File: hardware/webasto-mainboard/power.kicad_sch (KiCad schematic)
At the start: 14 parts, among them U5 BD9G341EFJ

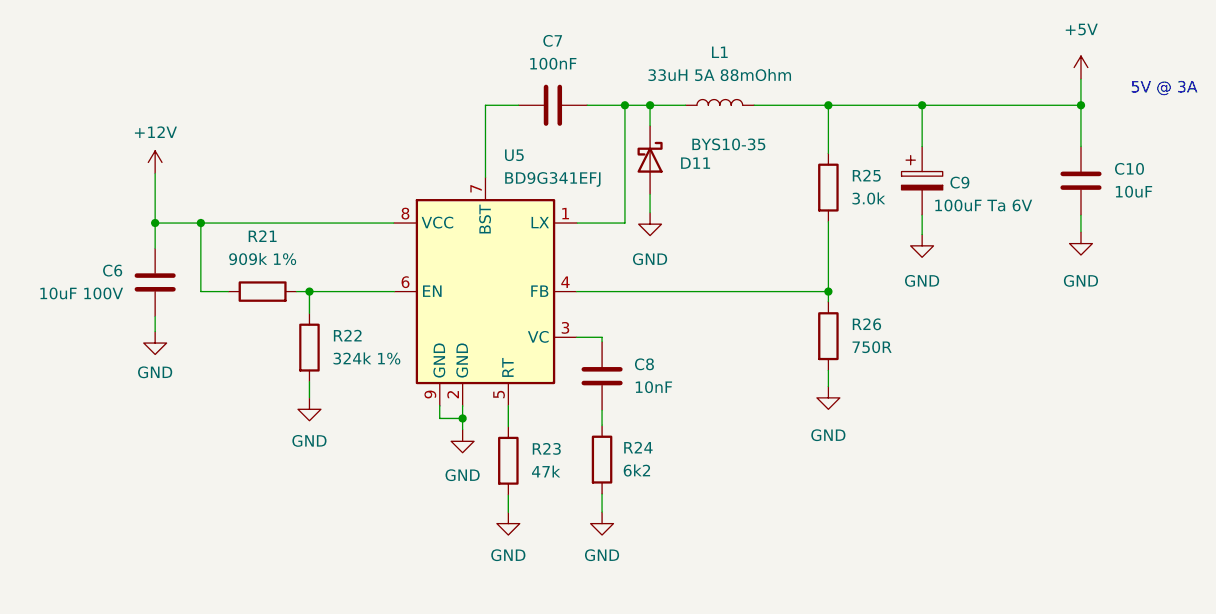
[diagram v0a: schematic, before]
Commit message: Move start/run to sensor board, add CANBUS
- WiFi is not being very helpful, and I'm concerned it won't work well once
  installed in the bus...  CANBus wiring is easy.
- Removed both Start/Run and the Vehicle Fan Relay from X1 to make space for
  canbus
- moved LEDs onto an I2C gpio extender.
- will need to still plumb in CAN_EN support
- will also need to yank out the WiFi stuff that won't stay stable anyways
  and reroute the CBOR out the CANBus instead of WiFi
- Vehicle Fan control will need to move to a LINBus fan controller board
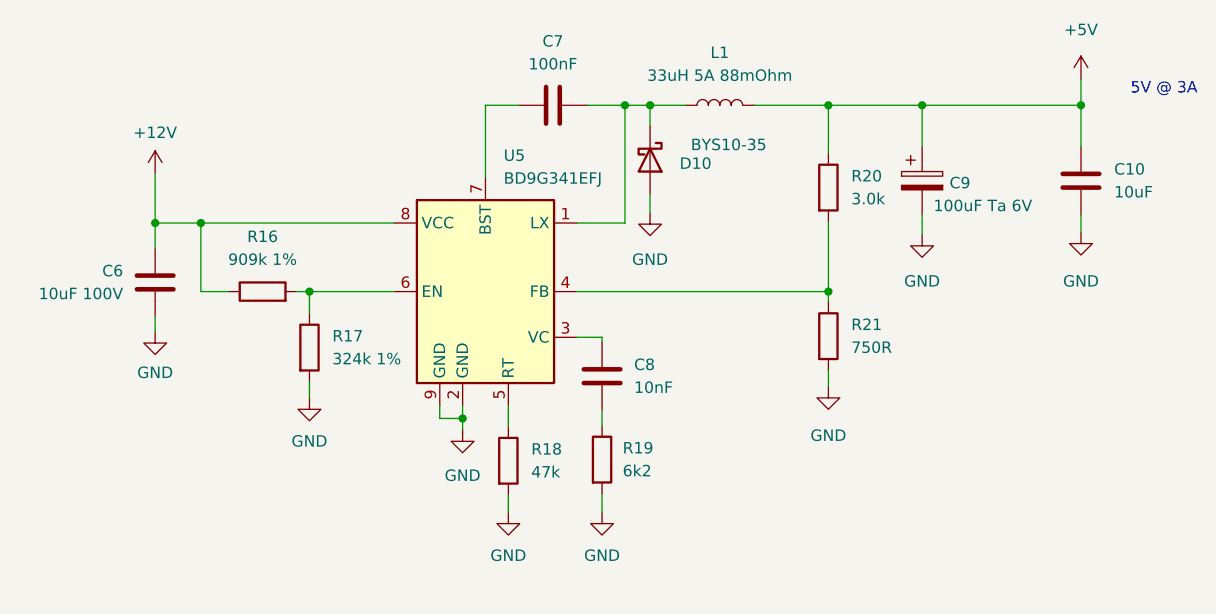
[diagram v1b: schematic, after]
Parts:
- renumbered D11 to D10, R21 to R16, R22 to R17, R23 to R18, R24 to R19, R25 to R20, R26 to R21
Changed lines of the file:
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@@
   (title_block
     (title "Webasto Replacement Mainboard (Thermo Top C)")
-    (date "2023-02-22")
+    (date "2023-02-23")
     (rev "2.0")
     (company "Gavin Hurlbut")
@@
   (symbol (lib_id "Device:D_Schottky") (at 163.068 65.278 270) (unit 1)
     (in_bom yes) (on_board yes)
-    (property "Reference" "D11" (id 0) (at 169.9006 65.659 90)
+    (property "Reference" "D10" (id 0) (at 169.9006 65.659 90)
       (effects (font (size 1.27 1.27)) (justify right))
     )
@@
   (symbol (lib_id "Device:R") (at 125.222 86.106 0) (unit 1)
     (in_bom yes) (on_board yes) (fields_autoplaced)
-    (property "Reference" "R22" (id 0) (at 127.762 84.8359 0)
+    (property "Reference" "R17" (id 0) (at 127.762 84.8359 0)
       (effects (font (size 1.27 1.27)) (justify left))
     )
@@
   (symbol (lib_id "power:GND") (at 210.947 73.279 0) (unit 1)
     (in_bom yes) (on_board yes) (fields_autoplaced)
-    (property "Reference" "#PWR061" (id 0) (at 210.947 79.629 0)
+    (property "Reference" "#PWR054" (id 0) (at 210.947 79.629 0)
       (effects (font (size 1.27 1.27)) hide)
     )
@@
   (symbol (lib_id "Device:R") (at 147.32 98.679 0) (unit 1)
     (in_bom yes) (on_board yes) (fields_autoplaced)
-    (property "Reference" "R23" (id 0) (at 149.86 97.4089 0)
+    (property "Reference" "R18" (id 0) (at 149.86 97.4089 0)
       (effects (font (size 1.27 1.27)) (justify left))
     )
@@
   (symbol (lib_id "power:GND") (at 163.068 71.12 0) (unit 1)
     (in_bom yes) (on_board yes) (fields_autoplaced)
-    (property "Reference" "#PWR057" (id 0) (at 163.068 77.47 0)
+    (property "Reference" "#PWR050" (id 0) (at 163.068 77.47 0)
       (effects (font (size 1.27 1.27)) hide)
     )
@@
   (symbol (lib_id "Device:R") (at 182.88 68.326 0) (unit 1)
     (in_bom yes) (on_board yes) (fields_autoplaced)
-    (property "Reference" "R25" (id 0) (at 185.42 67.0559 0)
+    (property "Reference" "R20" (id 0) (at 185.42 67.0559 0)
       (effects (font (size 1.27 1.27)) (justify left))
     )
@@
   (symbol (lib_id "power:GND") (at 193.294 73.533 0) (unit 1)
     (in_bom yes) (on_board yes) (fields_autoplaced)
-    (property "Reference" "#PWR059" (id 0) (at 193.294 79.883 0)
+    (property "Reference" "#PWR052" (id 0) (at 193.294 79.883 0)
       (effects (font (size 1.27 1.27)) hide)
     )
@@
   (symbol (lib_id "Device:R") (at 182.88 84.836 0) (unit 1)
     (in_bom yes) (on_board yes) (fields_autoplaced)
-    (property "Reference" "R26" (id 0) (at 185.42 83.5659 0)
+    (property "Reference" "R21" (id 0) (at 185.42 83.5659 0)
       (effects (font (size 1.27 1.27)) (justify left))
     )
@@
   (symbol (lib_id "power:GND") (at 108.077 84.328 0) (unit 1)
     (in_bom yes) (on_board yes) (fields_autoplaced)
-    (property "Reference" "#PWR052" (id 0) (at 108.077 90.678 0)
+    (property "Reference" "#PWR045" (id 0) (at 108.077 90.678 0)
       (effects (font (size 1.27 1.27)) hide)
     )
@@
   (symbol (lib_id "power:GND") (at 142.24 95.25 0) (unit 1)
     (in_bom yes) (on_board yes) (fields_autoplaced)
-    (property "Reference" "#PWR054" (id 0) (at 142.24 101.6 0)
+    (property "Reference" "#PWR047" (id 0) (at 142.24 101.6 0)
       (effects (font (size 1.27 1.27)) hide)
     )
@@
   (symbol (lib_id "power:GND") (at 125.222 91.694 0) (unit 1)
     (in_bom yes) (on_board yes) (fields_autoplaced)
-    (property "Reference" "#PWR053" (id 0) (at 125.222 98.044 0)
+    (property "Reference" "#PWR046" (id 0) (at 125.222 98.044 0)
       (effects (font (size 1.27 1.27)) hide)
     )
@@
   (symbol (lib_id "power:+12V") (at 108.077 66.802 0) (unit 1)
     (in_bom yes) (on_board yes) (fields_autoplaced)
-    (property "Reference" "#PWR051" (id 0) (at 108.077 70.612 0)
+    (property "Reference" "#PWR044" (id 0) (at 108.077 70.612 0)
       (effects (font (size 1.27 1.27)) hide)
     )
@@
   (symbol (lib_id "power:GND") (at 182.88 90.424 0) (unit 1)
     (in_bom yes) (on_board yes) (fields_autoplaced)
-    (property "Reference" "#PWR058" (id 0) (at 182.88 96.774 0)
+    (property "Reference" "#PWR051" (id 0) (at 182.88 96.774 0)
       (effects (font (size 1.27 1.27)) hide)
     )
@@
   (symbol (lib_id "power:+5V") (at 210.947 56.261 0) (unit 1)
     (in_bom yes) (on_board yes) (fields_autoplaced)
-    (property "Reference" "#PWR060" (id 0) (at 210.947 60.071 0)
+    (property "Reference" "#PWR053" (id 0) (at 210.947 60.071 0)
       (effects (font (size 1.27 1.27)) hide)
     )
@@
   (symbol (lib_id "Device:R") (at 120.015 79.883 90) (unit 1)
     (in_bom yes) (on_board yes) (fields_autoplaced)
-    (property "Reference" "R21" (id 0) (at 120.015 73.787 90))
+    (property "Reference" "R16" (id 0) (at 120.015 73.787 90))
     (property "Value" "909k 1%" (id 1) (at 120.015 76.327 90))
     (property "Footprint" "Resistor_SMD:R_0805_2012Metric_Pad1.20x1.40mm_HandSolder" (id 2) (at 120.015 81.661 90)
@@
   (symbol (lib_id "power:GND") (at 147.32 104.394 0) (unit 1)
     (in_bom yes) (on_board yes) (fields_autoplaced)
-    (property "Reference" "#PWR055" (id 0) (at 147.32 110.744 0)
+    (property "Reference" "#PWR048" (id 0) (at 147.32 110.744 0)
       (effects (font (size 1.27 1.27)) hide)
     )
@@
   (symbol (lib_id "Device:R") (at 157.734 98.552 0) (unit 1)
     (in_bom yes) (on_board yes) (fields_autoplaced)
-    (property "Reference" "R24" (id 0) (at 160.02 97.2819 0)
+    (property "Reference" "R19" (id 0) (at 160.02 97.2819 0)
       (effects (font (size 1.27 1.27)) (justify left))
     )
@@
   (symbol (lib_id "power:GND") (at 157.734 104.394 0) (unit 1)
     (in_bom yes) (on_board yes) (fields_autoplaced)
-    (property "Reference" "#PWR056" (id 0) (at 157.734 110.744 0)
-      (effects (font (size 1.27 1.27)) hide)
-    )
+    (property "Reference" "#PWR049" (id 0) (at 157.734 110.744 0)
+      (effects (font (size 1.27 1.27)) hide)
+    )

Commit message: Rejigger the mainboard to use voltage regulator
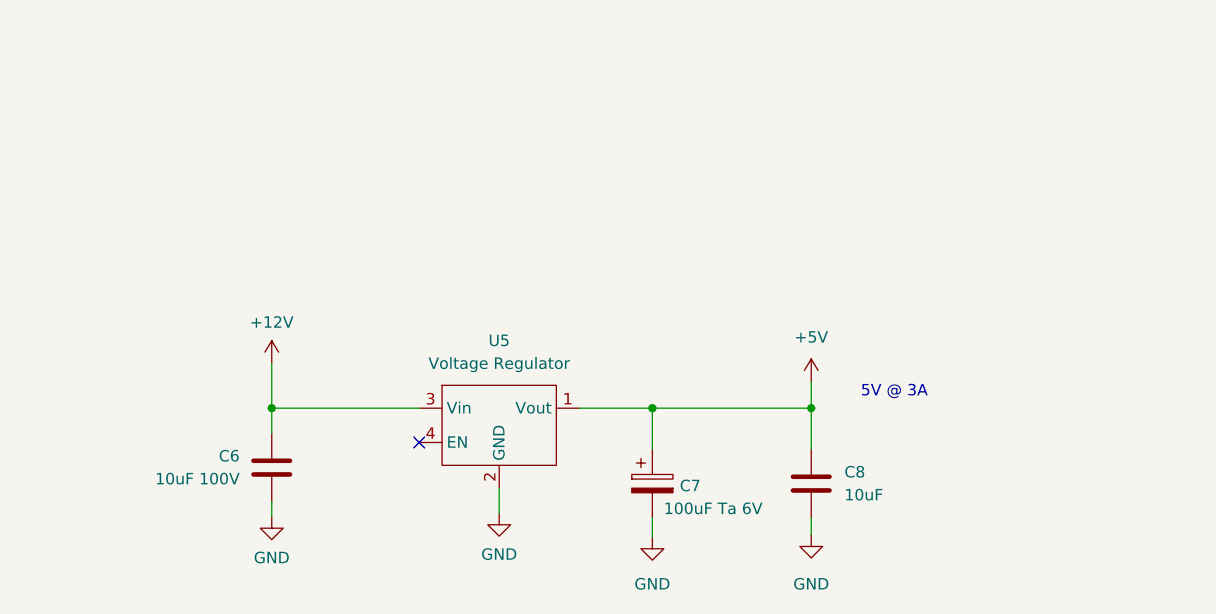
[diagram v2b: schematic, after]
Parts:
- removed C10: 10uF, Capacitor_SMD:C_0805_2012Metric, symbol Device:C
- removed C7: 100nF, Capacitor_SMD:C_0805_2012Metric, symbol Device:C
- removed C9: 100uF Ta 6V, Capacitor_Tantalum_SMD:CP_EIA-3216-10_Kemet-I_Pad1.58x1.35mm_HandSolder, symbol Device:C_Polarized
- removed D10: BYS10-35, Diode_SMD:D_SMA_Handsoldering, symbol Device:D_Schottky
- removed L1: 33uH 5A 88mOhm, UltraLibrarian:PM4346.333NLT, symbol Device:L
- removed R16: 909k 1%, Resistor_SMD:R_0805_2012Metric_Pad1.20x1.40mm_HandSolder, symbol Device:R
- removed R17: 324k 1%, Resistor_SMD:R_0805_2012Metric_Pad1.20x1.40mm_HandSolder, symbol Device:R
- removed R18: 47k, Resistor_SMD:R_0805_2012Metric_Pad1.20x1.40mm_HandSolder, symbol Device:R
- removed R19: 6k2, Resistor_SMD:R_0805_2012Metric_Pad1.20x1.40mm_HandSolder, symbol Device:R
- removed R20: 3.0k, Resistor_SMD:R_0805_2012Metric_Pad1.20x1.40mm_HandSolder, symbol Device:R
- removed R21: 750R, Resistor_SMD:R_0805_2012Metric_Pad1.20x1.40mm_HandSolder, symbol Device:R
- removed U5: BD9G341EFJ, Package_SO:HTSOP-8-1EP_3.9x4.9mm_P1.27mm_EP2.4x3.2mm_ThermalVias, symbol Beirdo:BD9G341EFJ
- added C7: 100uF Ta 6V, Capacitor_Tantalum_SMD:CP_EIA-3216-10_Kemet-I_Pad1.58x1.35mm_HandSolder, symbol Device:C_Polarized
- added U5: Voltage Regulator, Beirdo:Switching_Regulator_Module, symbol Beirdo:Switching_Regulator_Module
- C8: value 10nF -> 10uF; footprint Capacitor_SMD:C_0805_2012Metric -> Capacitor_SMD:C_0805_2012Metric_Pad1.18x1.45mm_HandSolder
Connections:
- net +12V: now also U5.3 (Vin)
- net +5V: now also C8.1, C7.1, U5.1 (Vout)
- net GND: now also C8.2, C7.2, U5.2 (GND)
- no-connect marks 0 -> 1
